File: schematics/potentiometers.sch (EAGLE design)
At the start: 22 parts, among them IC1 4011D, IC2 OPA642N, IC3 OPA642N

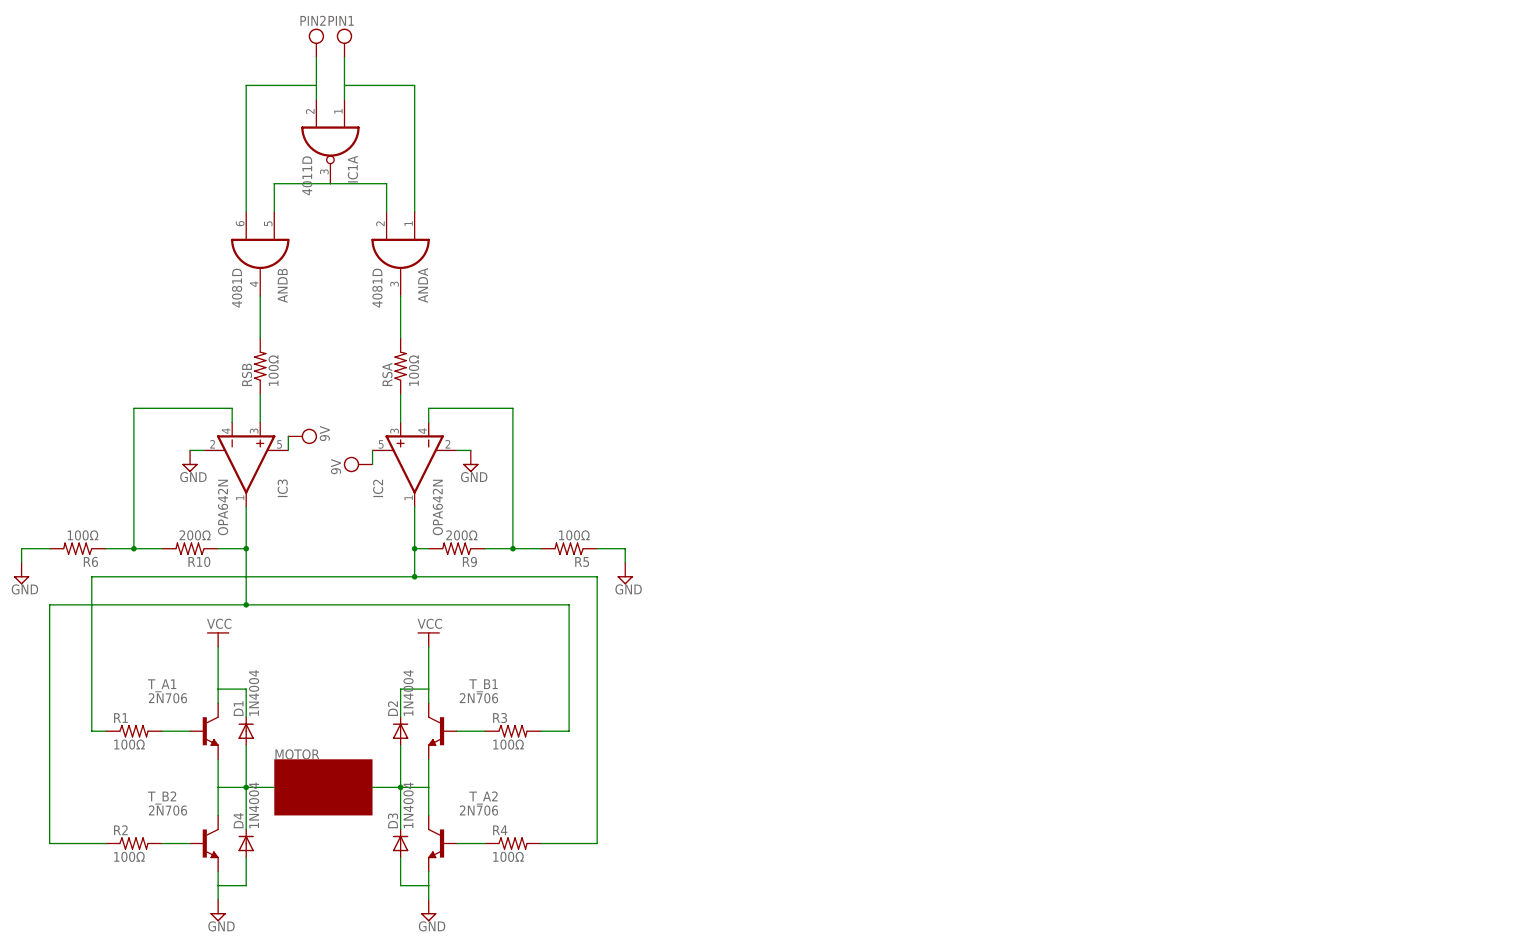
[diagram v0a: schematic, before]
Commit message: Worked on final proposal, started high-level diagram of circuitry.  Need button circuitry; will finish at next meeting.
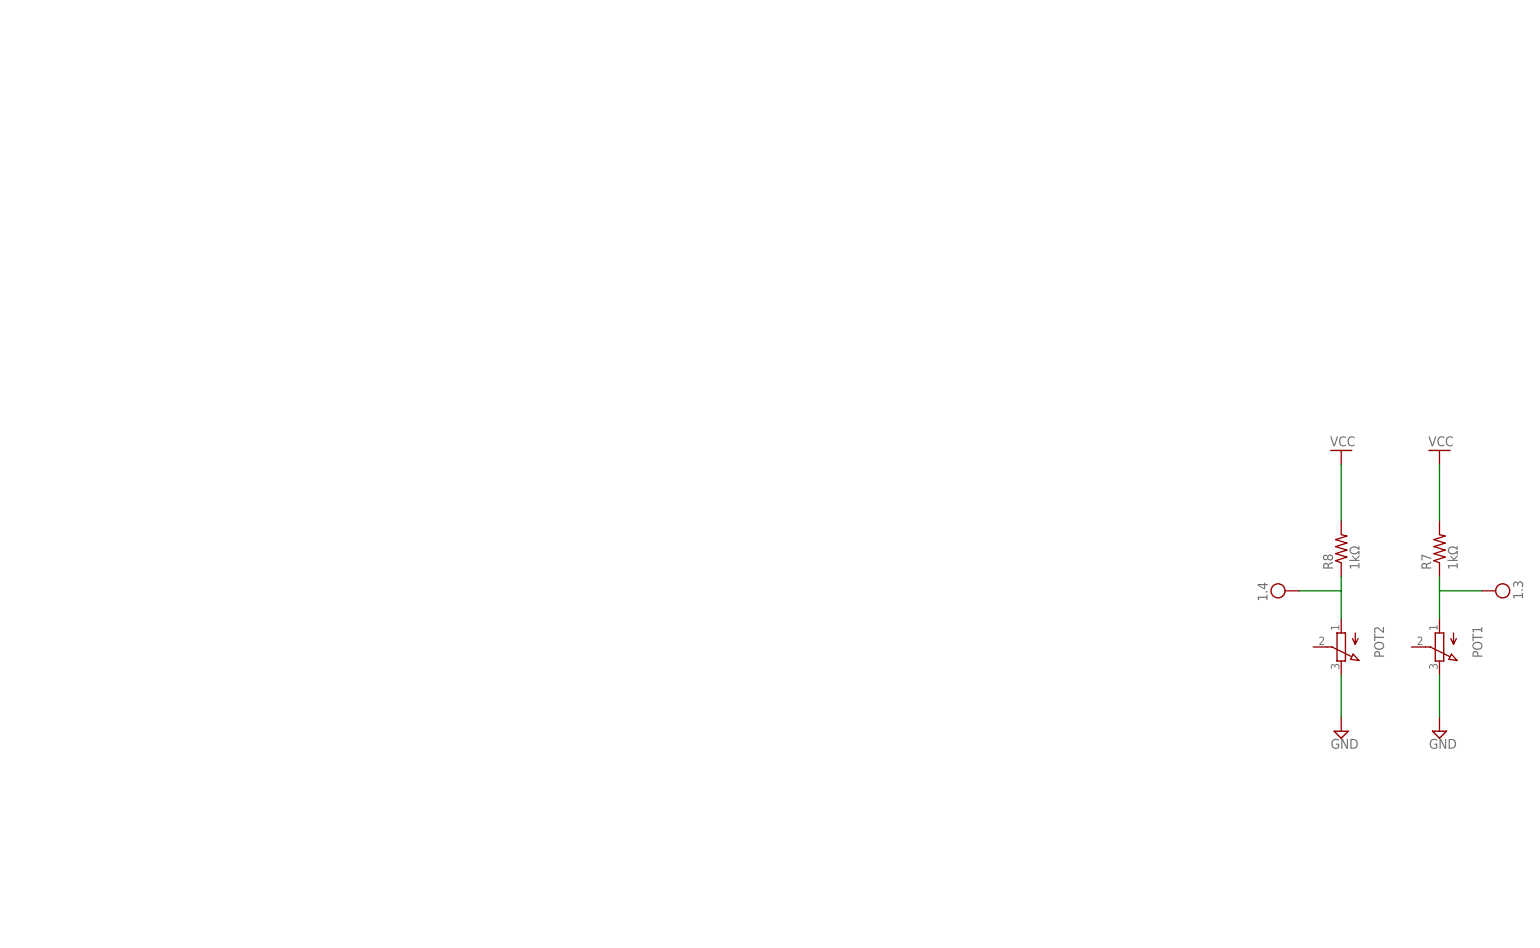
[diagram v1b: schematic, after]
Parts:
- removed AND: 4081D, 40xx:4081D
- removed D1, D2, D3, D4: 1N4004, diode:1N4004
- removed IC1: 4011D, 40xx:4011D
- removed IC2, IC3: OPA642N, burr-brown:OPA642N
- removed R1, R2, R3, R4, R5, R6, RSA, RSB: 100Ω, rcl:R-US_0204/2V
- removed R10, R9: 200Ω, rcl:R-US_0204/2V
- removed T_A1, T_A2, T_B1, T_B2: 2N706, transistor:2N706
- added POT1, POT2: (no value), pot:3RP/1610N
- added R7, R8: 1kΩ, rcl:R-US_0204/2V
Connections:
- removed net N$1: D2.A, D3.C, T_A2.C, T_B1.E
- removed net N$10: ANDB.O, RSB.2
- removed net N$11: ANDA.O, RSA.2
- removed net N$12: IC2.+IN, RSA.1
- removed net N$13: IC3.+IN, RSB.1
- removed net N$14: IC3.-IN, R10.2, R6.1
- removed net N$15: IC2.-IN, R5.2, R9.1
- removed net N$2: D1.A, D4.C, T_A1.E, T_B2.C
- removed net N$3: R4.1, T_A2.B
- removed net N$4: R3.1, T_B1.B
- removed net N$5: R1.2, T_A1.B
- removed net N$6: R2.2, T_B2.B
- removed net N$7: ANDA.I1, ANDB.I0, IC1A.O
- removed net N$8: IC3.OUT, R10.1, R2.1, R3.2
- removed net N$9: IC2.OUT, R1.1, R4.2, R9.2
- removed net VCC: D1.C, D2.C, IC2.V+, IC3.V+, T_A1.C, T_B1.C
- removed net VDD: ANDA.I0, ANDB.I1, IC1A.I0, IC1A.I1
- new net N$17: POT2.A, R8.1
- new net N$18: POT1.A, R7.1
- net GND: now also POT1.E, POT2.E, R7.2, R8.2; no longer D3.A, D4.A, IC2.V-, IC3.V-, R5.1, R6.2, T_A2.E, T_B2.E
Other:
- note removed: "MOTOR"

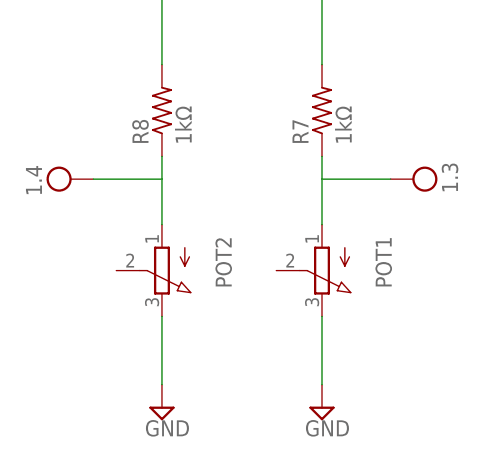
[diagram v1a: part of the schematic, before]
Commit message: Updated schematics to have appropriate pins and to fit most recent updates.  Final report updated and ready for review.
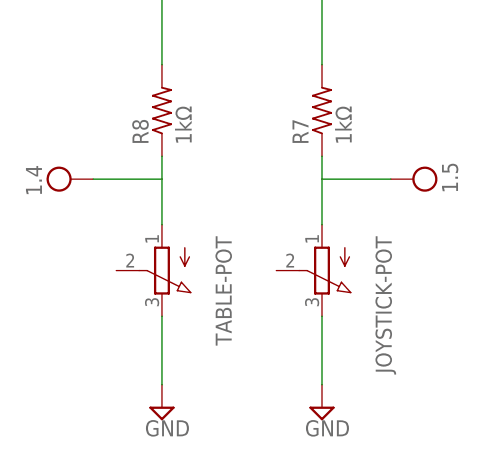
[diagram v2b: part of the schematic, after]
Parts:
- renumbered POT1 to JOYSTICK-POT, POT2 to TABLE-POT
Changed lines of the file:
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@@
 <part name="GND3" library="supply1" deviceset="GND" device="" value="VCC"/>
 <part name="SUPPLY9" library="supply2" deviceset="GND" device=""/>
-<part name="POT1" library="pot" deviceset="3RP/1610N" device=""/>
-<part name="SUPPLY10" library="supply2" deviceset="VCC" device="" value="1.3"/>
+<part name="JOYSTICK-POT" library="pot" deviceset="3RP/1610N" device=""/>
+<part name="SUPPLY10" library="supply2" deviceset="VCC" device="" value="1.5"/>
 <part name="R8" library="rcl" deviceset="R-US_" device="0204/2V" value="1kΩ"/>
 <part name="GND4" library="supply1" deviceset="GND" device="" value="VCC"/>
 <part name="SUPPLY11" library="supply2" deviceset="GND" device=""/>
-<part name="POT2" library="pot" deviceset="3RP/1610N" device=""/>
+<part name="TABLE-POT" library="pot" deviceset="3RP/1610N" device=""/>
 <part name="SUPPLY12" library="supply2" deviceset="VCC" device="" value="1.4"/>
 </parts>
@@
 <instance part="GND3" gate="1" x="58.42" y="76.2" rot="R180"/>
 <instance part="SUPPLY9" gate="GND" x="58.42" y="25.4"/>
-<instance part="POT1" gate="G$1" x="58.42" y="40.64" rot="R180"/>
+<instance part="JOYSTICK-POT" gate="G$1" x="58.42" y="40.64" rot="R180"/>
 <instance part="SUPPLY10" gate="G$1" x="68.58" y="50.8" rot="R270"/>
 <instance part="R8" gate="G$1" x="40.64" y="58.42" rot="R90"/>
 <instance part="GND4" gate="1" x="40.64" y="76.2" rot="R180"/>
 <instance part="SUPPLY11" gate="GND" x="40.64" y="25.4"/>
-<instance part="POT2" gate="G$1" x="40.64" y="40.64" rot="R180"/>
+<instance part="TABLE-POT" gate="G$1" x="40.64" y="40.64" rot="R180"/>
 <instance part="SUPPLY12" gate="G$1" x="30.48" y="50.8" rot="R90"/>
 </instances>
@@
 <net name="GND" class="0">
 <segment>
-<pinref part="POT1" gate="G$1" pin="E"/>
+<pinref part="JOYSTICK-POT" gate="G$1" pin="E"/>
 <pinref part="SUPPLY9" gate="GND" pin="GND"/>
 <wire x1="58.42" y1="35.56" x2="58.42" y2="27.94" width="0.1524" layer="91"/>
@@
 </segment>
 <segment>
-<pinref part="POT2" gate="G$1" pin="E"/>
+<pinref part="TABLE-POT" gate="G$1" pin="E"/>
 <pinref part="SUPPLY11" gate="GND" pin="GND"/>
 <wire x1="40.64" y1="35.56" x2="40.64" y2="27.94" width="0.1524" layer="91"/>
@@
 <net name="N$17" class="0">
 <segment>
-<pinref part="POT2" gate="G$1" pin="A"/>
+<pinref part="TABLE-POT" gate="G$1" pin="A"/>
 <pinref part="R8" gate="G$1" pin="1"/>
 <wire x1="40.64" y1="53.34" x2="40.64" y2="45.72" width="0.1524" layer="91"/>
@@
 <segment>
 <pinref part="R7" gate="G$1" pin="1"/>
-<pinref part="POT1" gate="G$1" pin="A"/>
+<pinref part="JOYSTICK-POT" gate="G$1" pin="A"/>
 <wire x1="58.42" y1="53.34" x2="58.42" y2="45.72" width="0.1524" layer="91"/>
 </segment>
